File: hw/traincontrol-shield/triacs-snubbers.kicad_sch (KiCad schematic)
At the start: 0 parts

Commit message: Phase 3+4 complete: implement all 8 schematics, fix KiCad 9 lib embedding
All 7 sub-sheets and top-level sheet fully implemented and validated with
kicad-cli (exit 0 on all 8 files).

Key fixes to lib_sym_entry() in generator scripts:
- Sub-symbol names must NOT include library prefix (KiCad 9 parser requirement)
- Local KiCad 6 library symbols upgraded inline: remove (id N) from properties,
  strip stroke colors, fix bare 'hide', add exclude_from_sim + embedded_fonts
- Derived symbols (MOC3021M extends MOC3010M) flattened by copying base
  graphics into derived, removing (extends ...) for standalone embedding

Validated: kicad-cli sch export netlist exits 0 for all 8 .kicad_sch files.

Co-Authored-By: Claude Sonnet 4.6 <noreply@anthropic.com>
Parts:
- added C7, C8: 10nF, Capacitor_SMD:C_0603_1608Metric, symbol Device:C
- added Q1, Q2: BT134W-600D, traincontrol-shield:SOT-223-3_L6.5-W3.4-P2.30-LS7.0-BR, symbol traincontrol-shield:BT134W-600D
- added R7, R8: 39Ω, Resistor_SMD:R_0603_1608Metric, symbol Device:R
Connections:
- new net AC_RTN: C7.2, C8.2, Q1.3 (G), Q2.3 (G)
- new net SN_A: C7.1, R7.2
- new net SN_B: C8.1, R8.2
- new net TRIAC_A_GATE: Q1.1 (T1)
- new net TRIAC_B_GATE: Q2.1 (T1)
- new net WINDING_A: Q1.2 (T2), Q1.4 (T2), R7.1
- new net WINDING_B: Q2.2 (T2), Q2.4 (T2), R8.1
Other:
- title: Traincontrol Shield — TRIACs + Snubbers -> TRIACs & Snubbers

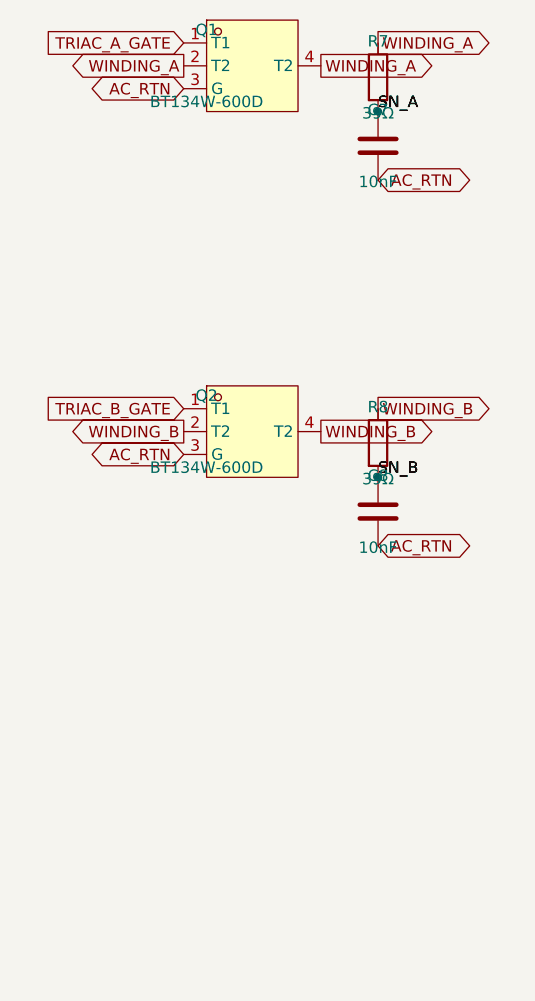
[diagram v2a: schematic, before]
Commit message: Add 2.54mm wire stubs to all power and global label connections
Power symbols (GND/+V) and global labels were placed directly on
component pins, making connections invisible in KiCad GUI. Add a
2.54mm stub wire between each component pin and power symbol/label
so connections are visually distinct. GND stubs go down (+y), +V
stubs go up (-y), label stubs go horizontally away from pin.
PWR_FLAG symbols are excluded (already have explicit wires).

All 8 schematics validate with kicad-cli exit 0.

Co-Authored-By: Claude Sonnet 4.6 <noreply@anthropic.com>
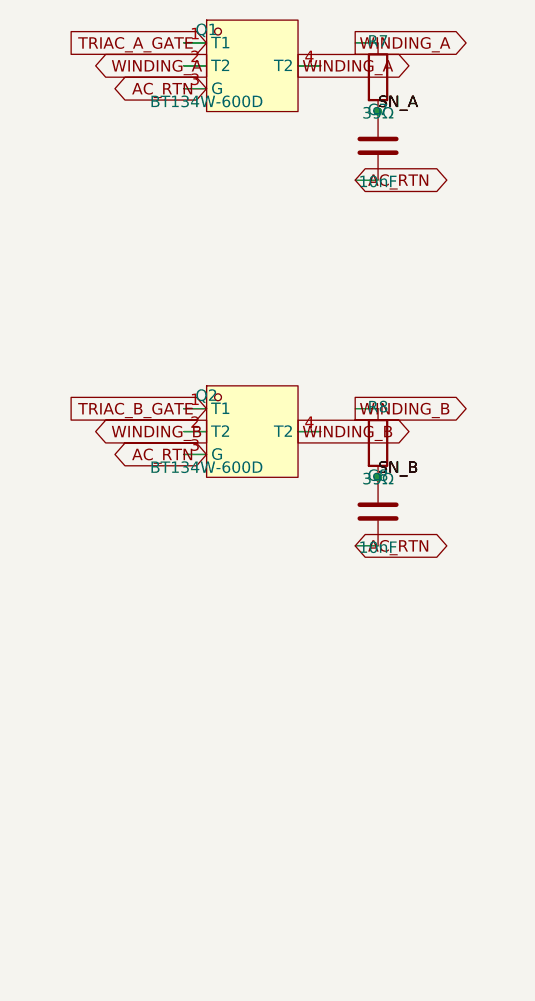
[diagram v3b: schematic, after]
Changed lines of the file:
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@@
 		)
+	)
+	(wire
+		(pts (xy 77.47 92.71000000000001) (xy 80.01 92.71000000000001))
+		(stroke (width 0) (type solid))
 	)
 	(global_label "AC_RTN"
 		(shape bidirectional)
-		(at 77.47 92.71000000000001 180)
-		(fields_autoplaced yes)
-		(effects (font (size 1.27 1.27)) (justify right bottom))
-		(property "Intersheetrefs" "${INTERSHEET_REFS}"
-			(at 77.47 92.71000000000001 0)
-			(effects (font (size 1.27 1.27)) (hide yes))
-		)
+		(at 80.01 92.71000000000001 180)
+		(fields_autoplaced yes)
+		(effects (font (size 1.27 1.27)) (justify right bottom))
+		(property "Intersheetrefs" "${INTERSHEET_REFS}"
+			(at 80.01 92.71000000000001 0)
+			(effects (font (size 1.27 1.27)) (hide yes))
+		)
+	)
+	(wire
+		(pts (xy 77.47 90.17) (xy 80.01 90.17))
+		(stroke (width 0) (type solid))
 	)
 	(global_label "WINDING_A"
 		(shape output)
-		(at 77.47 90.17 180)
-		(fields_autoplaced yes)
-		(effects (font (size 1.27 1.27)) (justify right bottom))
-		(property "Intersheetrefs" "${INTERSHEET_REFS}"
-			(at 77.47 90.17 0)
-			(effects (font (size 1.27 1.27)) (hide yes))
-		)
+		(at 80.01 90.17 180)
+		(fields_autoplaced yes)
+		(effects (font (size 1.27 1.27)) (justify right bottom))
+		(property "Intersheetrefs" "${INTERSHEET_REFS}"
+			(at 80.01 90.17 0)
+			(effects (font (size 1.27 1.27)) (hide yes))
+		)
+	)
+	(wire
+		(pts (xy 90.17 90.17) (xy 92.71000000000001 90.17))
+		(stroke (width 0) (type solid))
 	)
 	(global_label "WINDING_A"
 		(shape output)
-		(at 92.71000000000001 90.17 0)
-		(fields_autoplaced yes)
-		(effects (font (size 1.27 1.27)) (justify left bottom))
-		(property "Intersheetrefs" "${INTERSHEET_REFS}"
-			(at 92.71000000000001 90.17 0)
-			(effects (font (size 1.27 1.27)) (hide yes))
-		)
+		(at 90.17 90.17 0)
+		(fields_autoplaced yes)
+		(effects (font (size 1.27 1.27)) (justify left bottom))
+		(property "Intersheetrefs" "${INTERSHEET_REFS}"
+			(at 90.17 90.17 0)
+			(effects (font (size 1.27 1.27)) (hide yes))
+		)
+	)
+	(wire
+		(pts (xy 77.47 87.63) (xy 80.01 87.63))
+		(stroke (width 0) (type solid))
 	)
 	(global_label "TRIAC_A_GATE"
 		(shape input)
-		(at 77.47 87.63 180)
-		(fields_autoplaced yes)
-		(effects (font (size 1.27 1.27)) (justify right bottom))
-		(property "Intersheetrefs" "${INTERSHEET_REFS}"
-			(at 77.47 87.63 0)
+		(at 80.01 87.63 180)
+		(fields_autoplaced yes)
+		(effects (font (size 1.27 1.27)) (justify right bottom))
+		(property "Intersheetrefs" "${INTERSHEET_REFS}"
+			(at 80.01 87.63 0)
 			(effects (font (size 1.27 1.27)) (hide yes))
 		)
@@
 		)
 	)
+	(wire
+		(pts (xy 96.52 87.63) (xy 99.06 87.63))
+		(stroke (width 0) (type solid))
+	)
 	(global_label "WINDING_A"
 		(shape output)
-		(at 99.06 87.63 0)
-		(fields_autoplaced yes)
-		(effects (font (size 1.27 1.27)) (justify left bottom))
-		(property "Intersheetrefs" "${INTERSHEET_REFS}"
-			(at 99.06 87.63 0)
+		(at 96.52 87.63 0)
+		(fields_autoplaced yes)
+		(effects (font (size 1.27 1.27)) (justify left bottom))
+		(property "Intersheetrefs" "${INTERSHEET_REFS}"
+			(at 96.52 87.63 0)
 			(effects (font (size 1.27 1.27)) (hide yes))
 		)
@@
 		(effects (font (size 1.27 1.27)) (justify left bottom))
 	)
+	(wire
+		(pts (xy 96.52 102.87) (xy 99.06 102.87))
+		(stroke (width 0) (type solid))
+	)
 	(global_label "AC_RTN"
 		(shape bidirectional)
-		(at 99.06 102.87 0)
-		(fields_autoplaced yes)
-		(effects (font (size 1.27 1.27)) (justify left bottom))
-		(property "Intersheetrefs" "${INTERSHEET_REFS}"
-			(at 99.06 102.87 0)
+		(at 96.52 102.87 0)
+		(fields_autoplaced yes)
+		(effects (font (size 1.27 1.27)) (justify left bottom))
+		(property "Intersheetrefs" "${INTERSHEET_REFS}"
+			(at 96.52 102.87 0)
 			(effects (font (size 1.27 1.27)) (hide yes))
 		)
@@
 		)
 	)
+	(wire
+		(pts (xy 77.47 133.35) (xy 80.01 133.35))
+		(stroke (width 0) (type solid))
+	)
 	(global_label "AC_RTN"
 		(shape bidirectional)
-		(at 77.47 133.35 180)
-		(fields_autoplaced yes)
-		(effects (font (size 1.27 1.27)) (justify right bottom))
-		(property "Intersheetrefs" "${INTERSHEET_REFS}"
-			(at 77.47 133.35 0)
-			(effects (font (size 1.27 1.27)) (hide yes))
-		)
+		(at 80.01 133.35 180)
+		(fields_autoplaced yes)
+		(effects (font (size 1.27 1.27)) (justify right bottom))
+		(property "Intersheetrefs" "${INTERSHEET_REFS}"
+			(at 80.01 133.35 0)
+			(effects (font (size 1.27 1.27)) (hide yes))
+		)
+	)
+	(wire
+		(pts (xy 77.47 130.81) (xy 80.01 130.81))
+		(stroke (width 0) (type solid))
 	)
 	(global_label "WINDING_B"
 		(shape output)
-		(at 77.47 130.81 180)
-		(fields_autoplaced yes)
-		(effects (font (size 1.27 1.27)) (justify right bottom))
-		(property "Intersheetrefs" "${INTERSHEET_REFS}"
-			(at 77.47 130.81 0)
-			(effects (font (size 1.27 1.27)) (hide yes))
-		)
+		(at 80.01 130.81 180)
+		(fields_autoplaced yes)
+		(effects (font (size 1.27 1.27)) (justify right bottom))
+		(property "Intersheetrefs" "${INTERSHEET_REFS}"
+			(at 80.01 130.81 0)
+			(effects (font (size 1.27 1.27)) (hide yes))
+		)
+	)
+	(wire
+		(pts (xy 90.17 130.81) (xy 92.71000000000001 130.81))
+		(stroke (width 0) (type solid))
 	)
 	(global_label "WINDING_B"
 		(shape output)
-		(at 92.71000000000001 130.81 0)
-		(fields_autoplaced yes)
-		(effects (font (size 1.27 1.27)) (justify left bottom))
-		(property "Intersheetrefs" "${INTERSHEET_REFS}"
-			(at 92.71000000000001 130.81 0)
-			(effects (font (size 1.27 1.27)) (hide yes))
-		)
+		(at 90.17 130.81 0)
+		(fields_autoplaced yes)
+		(effects (font (size 1.27 1.27)) (justify left bottom))
+		(property "Intersheetrefs" "${INTERSHEET_REFS}"
+			(at 90.17 130.81 0)
+			(effects (font (size 1.27 1.27)) (hide yes))
+		)
+	)
+	(wire
+		(pts (xy 77.47 128.27) (xy 80.01 128.27))
+		(stroke (width 0) (type solid))
 	)
 	(global_label "TRIAC_B_GATE"
 		(shape input)
-		(at 77.47 128.27 180)
-		(fields_autoplaced yes)
-		(effects (font (size 1.27 1.27)) (justify right bottom))
-		(property "Intersheetrefs" "${INTERSHEET_REFS}"
-			(at 77.47 128.27 0)
+		(at 80.01 128.27 180)
+		(fields_autoplaced yes)
+		(effects (font (size 1.27 1.27)) (justify right bottom))
+		(property "Intersheetrefs" "${INTERSHEET_REFS}"
+			(at 80.01 128.27 0)
 			(effects (font (size 1.27 1.27)) (hide yes))
 		)
@@
 		)
 	)
+	(wire
+		(pts (xy 96.52 128.27) (xy 99.06 128.27))
+		(stroke (width 0) (type solid))
+	)
 	(global_label "WINDING_B"
 		(shape output)
-		(at 99.06 128.27 0)
-		(fields_autoplaced yes)
-		(effects (font (size 1.27 1.27)) (justify left bottom))
-		(property "Intersheetrefs" "${INTERSHEET_REFS}"
-			(at 99.06 128.27 0)
+		(at 96.52 128.27 0)
+		(fields_autoplaced yes)
+		(effects (font (size 1.27 1.27)) (justify left bottom))
+		(property "Intersheetrefs" "${INTERSHEET_REFS}"
+			(at 96.52 128.27 0)
 			(effects (font (size 1.27 1.27)) (hide yes))
 		)
@@
 		(effects (font (size 1.27 1.27)) (justify left bottom))
 	)
+	(wire
+		(pts (xy 96.52 143.51000000000002) (xy 99.06 143.51000000000002))
+		(stroke (width 0) (type solid))
+	)
 	(global_label "AC_RTN"
 		(shape bidirectional)
-		(at 99.06 143.51000000000002 0)
-		(fields_autoplaced yes)
-		(effects (font (size 1.27 1.27)) (justify left bottom))
-		(property "Intersheetrefs" "${INTERSHEET_REFS}"
-			(at 99.06 143.51000000000002 0)
-			(effects (font (size 1.27 1.27)) (hide yes))
-		)
+		(at 96.52 143.51000000000002 0)
+		(fields_autoplaced yes)
+		(effects (font (size 1.27 1.27)) (justify left bottom))
+		(property "Intersheetrefs" "${INTERSHEET_REFS}"
+			(at 96.52 143.51000000000002 0)
+			(effects (font (size 1.27 1.27)) (hide yes))
+		)

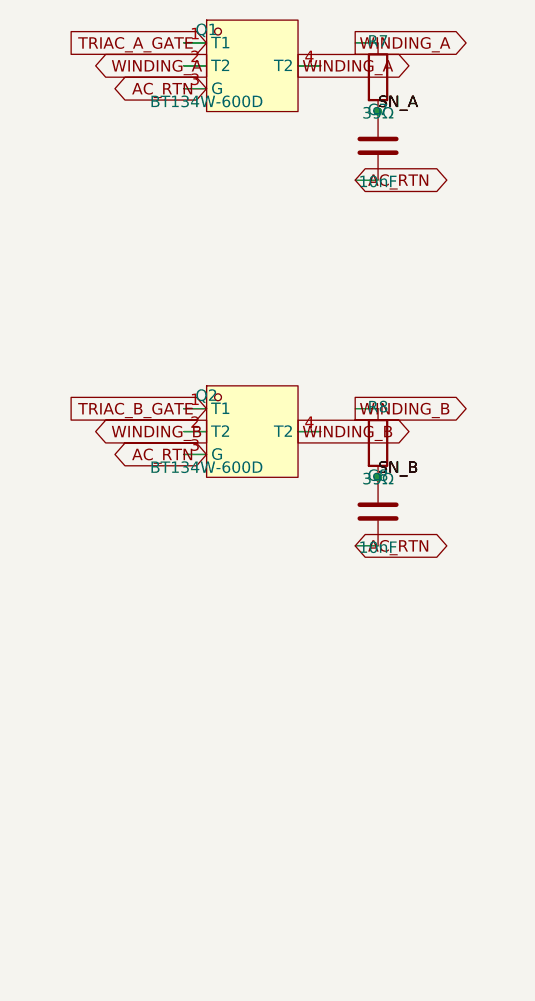
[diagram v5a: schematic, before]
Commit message: Add hierarchical ports to all sub-sheets and top-level connections
Replace inter-sheet global_label elements with hierarchical_label in all
sub-sheets, so each sheet exports visible ports on its sheet box symbol
in the top-level. Add matching (pin ...) entries to every sheet block in
the top-level. Connect all sheet pins with bidirectional global_labels in
the inter-column gap (x=105..120) so named nets auto-join.

Port counts per sub-sheet:
  power-supply:       2  (AC_IN, AC_RTN)
  zero-crossing:      3  (AC_IN, AC_RTN, ZC_OUT)
  xor-interlock:      6  (CTRL_A×2, CTRL_B×2, PHASE_A, PHASE_B)
  opto-triac-drive:   6  (PHASE_A, PHASE_B, AC_RTN×2, TRIAC_A_GATE, TRIAC_B_GATE)
  triacs-snubbers:   12  (AC_RTN×2, WINDING_A×3, WINDING_B×3, TRIAC_A_GATE, TRIAC_B_GATE)
  rail-voltage-sense: 1  (VSENSE)
  mcu:                4  (CTRL_A, CTRL_B, ZC_OUT, VSENSE)

All 8 schematics validate: kicad-cli exit 0.
Fix: correct KiCad 9 keyword is `hierarchical_label`, not `hier_label`.

Co-Authored-By: Claude Sonnet 4.6 <noreply@anthropic.com>
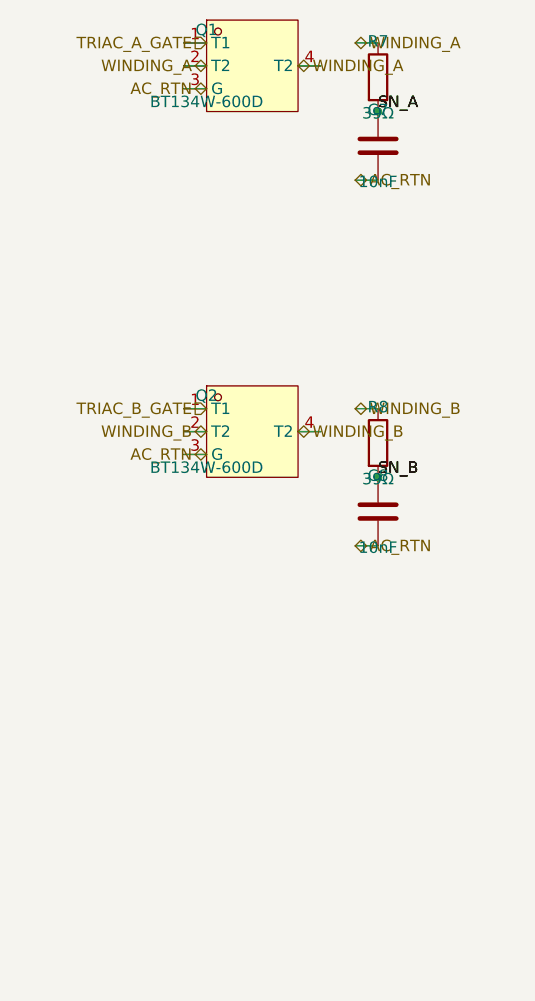
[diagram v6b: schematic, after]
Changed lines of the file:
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@@
 		(stroke (width 0) (type solid))
 	)
-	(global_label "AC_RTN"
+	(hierarchical_label "AC_RTN"
 		(shape bidirectional)
 		(at 80.01 92.71000000000001 180)
@@
 		(stroke (width 0) (type solid))
 	)
-	(global_label "WINDING_A"
-		(shape output)
+	(hierarchical_label "WINDING_A"
+		(shape bidirectional)
 		(at 80.01 90.17 180)
 		(fields_autoplaced yes)
@@
 		(stroke (width 0) (type solid))
 	)
-	(global_label "WINDING_A"
-		(shape output)
+	(hierarchical_label "WINDING_A"
+		(shape bidirectional)
 		(at 90.17 90.17 0)
 		(fields_autoplaced yes)
@@
 		(stroke (width 0) (type solid))
 	)
-	(global_label "TRIAC_A_GATE"
+	(hierarchical_label "TRIAC_A_GATE"
 		(shape input)
 		(at 80.01 87.63 180)
@@
 		(stroke (width 0) (type solid))
 	)
-	(global_label "WINDING_A"
-		(shape output)
+	(hierarchical_label "WINDING_A"
+		(shape bidirectional)
 		(at 96.52 87.63 0)
 		(fields_autoplaced yes)
@@
 		(stroke (width 0) (type solid))
 	)
-	(global_label "AC_RTN"
+	(hierarchical_label "AC_RTN"
 		(shape bidirectional)
 		(at 96.52 102.87 0)
@@
 		(stroke (width 0) (type solid))
 	)
-	(global_label "AC_RTN"
+	(hierarchical_label "AC_RTN"
 		(shape bidirectional)
 		(at 80.01 133.35 180)
@@
 		(stroke (width 0) (type solid))
 	)
-	(global_label "WINDING_B"
-		(shape output)
+	(hierarchical_label "WINDING_B"
+		(shape bidirectional)
 		(at 80.01 130.81 180)
 		(fields_autoplaced yes)
@@
 		(stroke (width 0) (type solid))
 	)
-	(global_label "WINDING_B"
-		(shape output)
+	(hierarchical_label "WINDING_B"
+		(shape bidirectional)
 		(at 90.17 130.81 0)
 		(fields_autoplaced yes)
@@
 		(stroke (width 0) (type solid))
 	)
-	(global_label "TRIAC_B_GATE"
+	(hierarchical_label "TRIAC_B_GATE"
 		(shape input)
 		(at 80.01 128.27 180)
@@
 		(stroke (width 0) (type solid))
 	)
-	(global_label "WINDING_B"
-		(shape output)
+	(hierarchical_label "WINDING_B"
+		(shape bidirectional)
 		(at 96.52 128.27 0)
 		(fields_autoplaced yes)
@@
 		(stroke (width 0) (type solid))
 	)
-	(global_label "AC_RTN"
+	(hierarchical_label "AC_RTN"
 		(shape bidirectional)
 		(at 96.52 143.51000000000002 0)

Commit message: Disperse component layout and triple wire stub length across all sheets
- STUB: 2.54 → 7.62 mm (3×) in all three generator scripts
- Inter-component spacing doubled in power-supply, MCU, and logic sheets
- Top-level inter-column gap widened (LX 120 → 130 mm) to avoid label collision
- Sheet frame heights made variable per pin count (20–35 mm)
- Right-column sheet x-origin and connector J4/J5/J6 x-positions updated accordingly
- All 8 sheets regenerated and validated with kicad-cli

Co-Authored-By: Claude Sonnet 4.6 <noreply@anthropic.com>
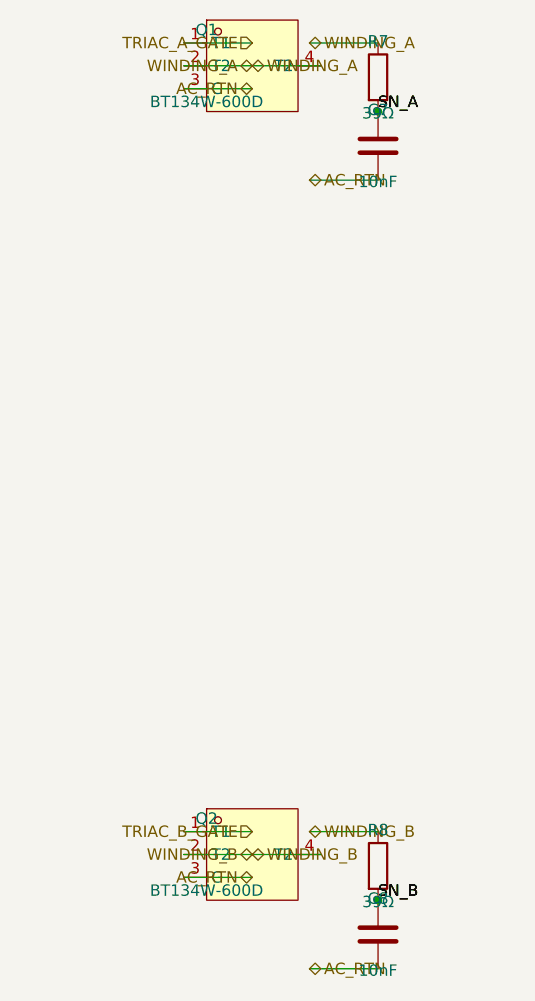
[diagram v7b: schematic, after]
